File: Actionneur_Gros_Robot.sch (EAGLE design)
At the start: 52 parts, among them M1 ARDUINO-NANO-3.0, M10 SERVO, M11 SERVO, M2 SERVO, M3 SERVO, M4 SERVO, M5 SERVO, M6 SERVO, M7 SERVO, M8 SERVO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

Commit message: revA3
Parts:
- added R19: 15K, rcl:R-EU_0207/7
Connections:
- new net N$15: R19.1, U$2.RS
- net GND: now also R19.2
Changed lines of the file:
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@@
 <part name="R18" library="rcl" library_urn="urn:adsk.eagle:library:334" deviceset="R-EU_" device="0207/7" package3d_urn="urn:adsk.eagle:package:23493/2" value="10K"/>
 <part name="P+20" library="supply1" library_urn="urn:adsk.eagle:library:371" deviceset="VCC" device=""/>
+<part name="R19" library="rcl" library_urn="urn:adsk.eagle:library:334" deviceset="R-EU_" device="0207/7" package3d_urn="urn:adsk.eagle:package:23493/2" value="15K"/>
+<part name="GND24" library="supply1" library_urn="urn:adsk.eagle:library:371" deviceset="GND" device=""/>
 </parts>
 <sheets>
@@
 <attribute name="VALUE" x="9.906" y="59.182" size="1.778" layer="96" rot="R90"/>
 </instance>
+<instance part="R19" gate="G$1" x="96.342" y="54.67" smashed="yes" rot="R180">
+<attribute name="NAME" x="100.152" y="53.1714" size="1.778" layer="95" rot="R180"/>
+<attribute name="VALUE" x="100.152" y="57.972" size="1.778" layer="96" rot="R180"/>
+</instance>
+<instance part="GND24" gate="1" x="73.268" y="47.258" smashed="yes">
+<attribute name="VALUE" x="70.728" y="44.718" size="1.778" layer="96"/>
+</instance>
 </instances>
 <busses>
@@
 <wire x1="15.436" y1="22.096" x2="15.324" y2="19.81" width="0.1524" layer="91"/>
 </segment>
+<segment>
+<pinref part="GND24" gate="1" pin="GND"/>
+<pinref part="R19" gate="G$1" pin="2"/>
+<wire x1="73.268" y1="49.798" x2="73.268" y2="54.67" width="0.1524" layer="91"/>
+<wire x1="73.268" y1="54.67" x2="91.262" y2="54.67" width="0.1524" layer="91"/>
+</segment>
 </net>
 <net name="VDD" class="0">
@@
 </segment>
 </net>
+<net name="N$15" class="0">
+<segment>
+<pinref part="U$2" gate="A" pin="RS"/>
+<pinref part="R19" gate="G$1" pin="1"/>
+<wire x1="107.22" y1="46.62" x2="101.422" y2="46.62" width="0.1524" layer="91"/>
+<wire x1="101.422" y1="46.62" x2="101.422" y2="54.67" width="0.1524" layer="91"/>
+</segment>
+</net>

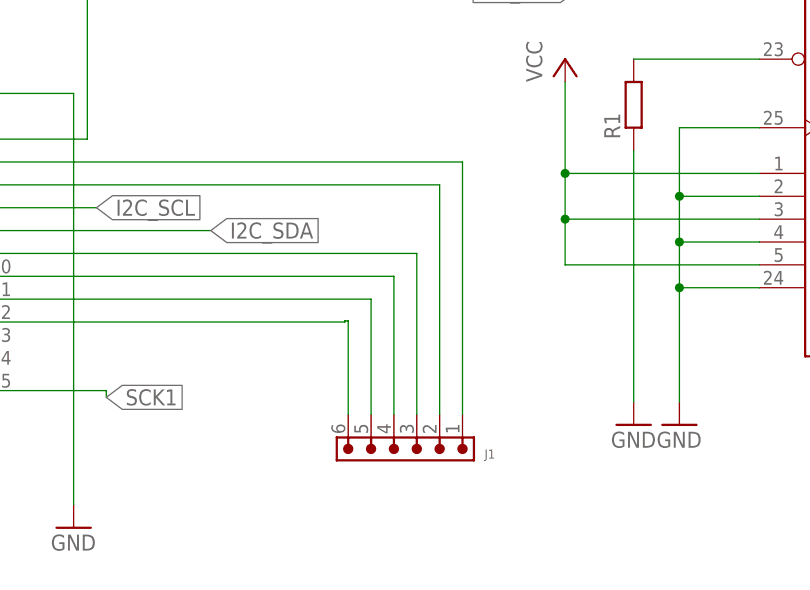
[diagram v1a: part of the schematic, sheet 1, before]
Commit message: Added testpins for CANH and CANL
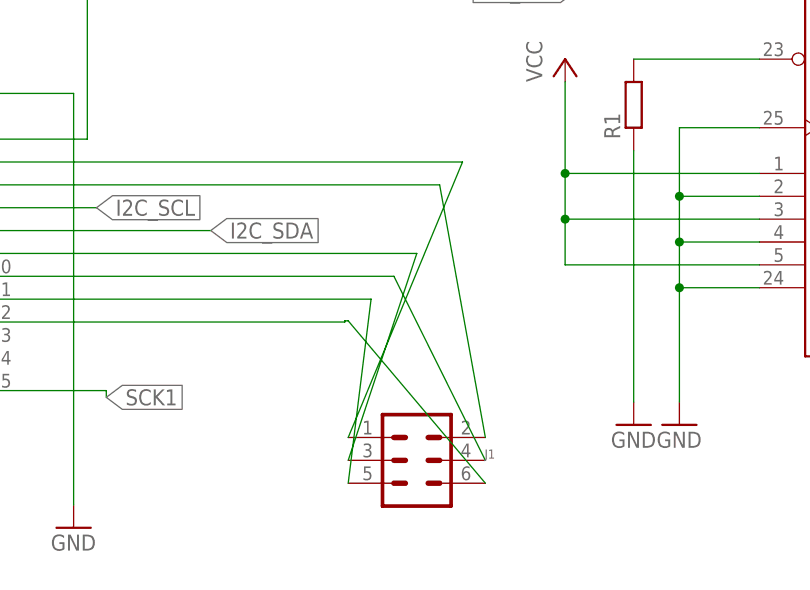
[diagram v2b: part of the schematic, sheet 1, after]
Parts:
- added TP1, TP2: PTR1PAD1-17, testpad:PTR1PAD1-17
- J1: device Wurth_Connectors_WR-PHD:6200XX11121_62000611121 -> con-lstb:MA03-2
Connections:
- net CANH: now also TP1.TP
- net CANL: now also TP2.TP
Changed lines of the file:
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@@
 <part name="P+15" library="supply1" library_urn="urn:adsk.eagle:library:371" deviceset="VCC" device=""/>
 <part name="R13" library="rcl" library_urn="urn:adsk.eagle:library:334" deviceset="R-EU_" device="0204/7" package3d_urn="urn:adsk.eagle:package:23498/2"/>
-<part name="J1" library="Wurth_Connectors_WR-PHD" library_urn="urn:adsk.eagle:library:14804658" deviceset="6200XX11121_62000611121" device="" package3d_urn="urn:adsk.eagle:package:14805729/2"/>
+<part name="J1" library="con-lstb" library_urn="urn:adsk.eagle:library:162" deviceset="MA03-2" device="" package3d_urn="urn:adsk.eagle:package:8334/1"/>
 <part name="J2" library="con-lstb" library_urn="urn:adsk.eagle:library:162" deviceset="MA04-2" device="" package3d_urn="urn:adsk.eagle:package:8368/1"/>
 <part name="FRAME2" library="frames" library_urn="urn:adsk.eagle:library:229" deviceset="A4L-LOC" device=""/>
@@
 <part name="R19" library="rcl" library_urn="urn:adsk.eagle:library:334" deviceset="R-EU_" device="0207/7" package3d_urn="urn:adsk.eagle:package:23493/2" value="15K"/>
 <part name="GND24" library="supply1" library_urn="urn:adsk.eagle:library:371" deviceset="GND" device=""/>
+<part name="TP1" library="testpad" library_urn="urn:adsk.eagle:library:385" deviceset="PTR1" device="PAD1-17" package3d_urn="urn:adsk.eagle:package:27949/1"/>
+<part name="TP2" library="testpad" library_urn="urn:adsk.eagle:library:385" deviceset="PTR1" device="PAD1-17" package3d_urn="urn:adsk.eagle:package:27949/1"/>
 </parts>
 <sheets>
@@
 <attribute name="VALUE" x="207.01" y="114.808" size="1.778" layer="96"/>
 </instance>
-<instance part="J1" gate="G$1" x="141" y="24" smashed="yes" rot="R180">
+<instance part="J1" gate="1" x="141" y="24" smashed="yes" rot="R180">
 <attribute name="NAME" x="148.53" y="25.205" size="1.016" layer="95" rot="R180" align="bottom-right"/>
 <attribute name="VALUE" x="148.49" y="27.01" size="1.016" layer="96" rot="R180" align="bottom-right"/>
@@
 <wire x1="93.98" y1="39.37" x2="133" y2="39.37" width="0.1524" layer="91"/>
 <wire x1="133" y1="39.37" x2="133" y2="39.5" width="0.1524" layer="91"/>
-<pinref part="J1" gate="G$1" pin="6"/>
+<pinref part="J1" gate="1" pin="6"/>
 <wire x1="133" y1="39.5" x2="133.38" y2="39.5" width="0.1524" layer="91"/>
-<wire x1="133.38" y1="39.5" x2="133.38" y2="29.08" width="0.1524" layer="91"/>
+<wire x1="133.38" y1="39.5" x2="148.62" y2="21.46" width="0.1524" layer="91"/>
 </segment>
 </net>
@@
 <segment>
 <pinref part="M1" gate="G$1" pin="A1"/>
-<pinref part="J1" gate="G$1" pin="5"/>
+<pinref part="J1" gate="1" pin="5"/>
 <wire x1="93.98" y1="41.91" x2="135.92" y2="41.91" width="0.1524" layer="91"/>
-<wire x1="135.92" y1="41.91" x2="135.92" y2="29.08" width="0.1524" layer="91"/>
+<wire x1="135.92" y1="41.91" x2="133.38" y2="21.46" width="0.1524" layer="91"/>
 </segment>
 </net>
@@
 <segment>
 <pinref part="M1" gate="G$1" pin="A3"/>
-<pinref part="J1" gate="G$1" pin="3"/>
+<pinref part="J1" gate="1" pin="3"/>
 <wire x1="93.98" y1="46.99" x2="141" y2="46.99" width="0.1524" layer="91"/>
-<wire x1="141" y1="46.99" x2="141" y2="29.08" width="0.1524" layer="91"/>
+<wire x1="141" y1="46.99" x2="133.38" y2="24" width="0.1524" layer="91"/>
 </segment>
 </net>
@@
 <segment>
 <pinref part="M1" gate="G$1" pin="A2"/>
-<pinref part="J1" gate="G$1" pin="4"/>
+<pinref part="J1" gate="1" pin="4"/>
 <wire x1="93.98" y1="44.45" x2="138.46" y2="44.45" width="0.1524" layer="91"/>
-<wire x1="138.46" y1="44.45" x2="138.46" y2="29.08" width="0.1524" layer="91"/>
+<wire x1="138.46" y1="44.45" x2="148.62" y2="24" width="0.1524" layer="91"/>
 </segment>
 </net>
@@
 <segment>
 <pinref part="M1" gate="G$1" pin="A6"/>
-<pinref part="J1" gate="G$1" pin="2"/>
+<pinref part="J1" gate="1" pin="2"/>
 <wire x1="93.98" y1="54.61" x2="143.54" y2="54.61" width="0.1524" layer="91"/>
-<wire x1="143.54" y1="54.61" x2="143.54" y2="29.08" width="0.1524" layer="91"/>
+<wire x1="143.54" y1="54.61" x2="148.62" y2="26.54" width="0.1524" layer="91"/>
 </segment>
 </net>
@@
 <segment>
 <pinref part="M1" gate="G$1" pin="A7"/>
-<pinref part="J1" gate="G$1" pin="1"/>
+<pinref part="J1" gate="1" pin="1"/>
 <wire x1="93.98" y1="57.15" x2="146.08" y2="57.15" width="0.1524" layer="91"/>
-<wire x1="146.08" y1="57.15" x2="146.08" y2="29.08" width="0.1524" layer="91"/>
+<wire x1="146.08" y1="57.15" x2="133.38" y2="26.54" width="0.1524" layer="91"/>
 </segment>
 </net>
@@
 <attribute name="VALUE" x="70.728" y="44.718" size="1.778" layer="96"/>
 </instance>
+<instance part="TP1" gate="G$1" x="87.63" y="19.304" smashed="yes">
+<attribute name="NAME" x="86.614" y="12.954" size="1.778" layer="95" rot="R90"/>
+<attribute name="TP_SIGNAL_NAME" x="88.9" y="16.764" size="1.778" layer="97"/>
+</instance>
+<instance part="TP2" gate="G$1" x="96.266" y="19.304" smashed="yes">
+<attribute name="NAME" x="95.25" y="12.954" size="1.778" layer="95" rot="R90"/>
+<attribute name="TP_SIGNAL_NAME" x="97.536" y="16.764" size="1.778" layer="97"/>
+</instance>
 </instances>
 <busses>
@@
 <wire x1="75.5" y1="41.5" x2="91.5" y2="41.5" width="0.1524" layer="91"/>
 <wire x1="91.5" y1="41.5" x2="91.5" y2="41.58" width="0.1524" layer="91"/>
+<wire x1="107.22" y1="39" x2="96.266" y2="39" width="0.1524" layer="91"/>
+<wire x1="96.266" y1="39" x2="96.266" y2="24.384" width="0.1524" layer="91"/>
+<junction x="107.22" y="39"/>
+<wire x1="96.266" y1="24.384" x2="87.63" y2="24.384" width="0.1524" layer="91"/>
+<pinref part="TP1" gate="G$1" pin="TP"/>
+<wire x1="87.63" y1="24.384" x2="87.63" y2="21.844" width="0.1524" layer="91"/>
 </segment>
 </net>
@@
 <wire x1="59.5" y1="31.42" x2="91.5" y2="31.42" width="0.1524" layer="91"/>
 <junction x="91.5" y="31.42"/>
-</segment>
-</net>
+<pinref part="TP2" gate="G$1" pin="TP"/>
+<wire x1="96.266" y1="21.844" x2="107.22" y2="21.844" width="0.1524" layer="91"/>
+<wire x1="107.22" y1="21.844" x2="107.22" y2="33.92" width="0.1524" layer="91"/>
+<junction x="107.22" y="33.92"/>
+</segment>
+</net>
